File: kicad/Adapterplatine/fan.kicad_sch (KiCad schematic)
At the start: 15 parts, among them J2 Conn_01x05_Pin, J3 Conn_01x04_Pin, J4 Conn_01x03_Pin, X25_1 Conn_01x02_Pin, X36B1 DE9_Socket, X38 Conn_01x02_Pin, X44 Conn_01x05_Pin, X44__g1 Conn_01x02_Pin, X44__r1 Conn_01x04_Pin, X44__y1 Conn_01x02_Pin, X44_b1 Conn_01x04_Pin

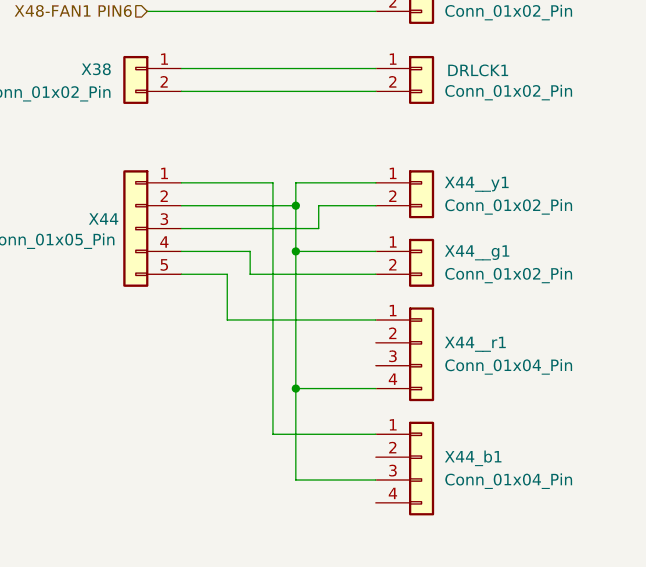
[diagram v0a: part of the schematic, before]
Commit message: Leitungsverlegung Adapterplatine abgeschlossen
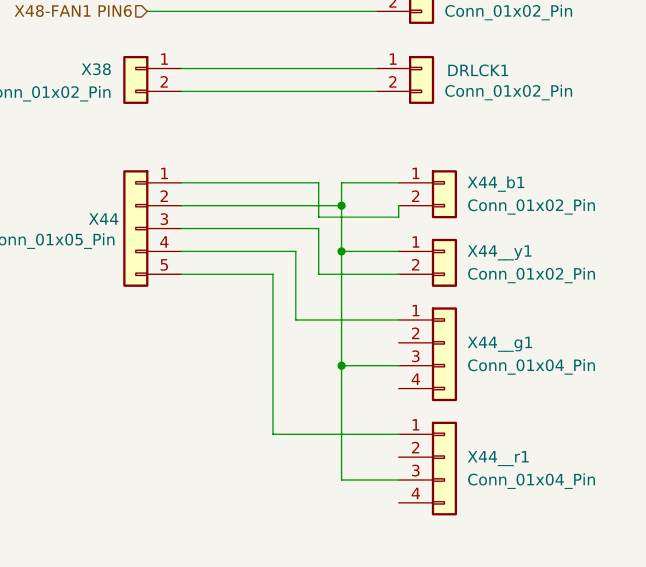
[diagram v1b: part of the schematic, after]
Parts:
- X44__g1: value Conn_01x02_Pin -> Conn_01x04_Pin; footprint Connector_JST:JST_XH_B2B-XH-A_1x02_P2.50mm_Vertical -> Connector_Molex:Molex_KK-254_AE-6410-04A_1x04_P2.54mm_Vertical; symbol Connector_Generic:Conn_01x02 -> Connector_Generic:Conn_01x04
- X44_b1: value Conn_01x04_Pin -> Conn_01x02_Pin; footprint Connector_Molex:Molex_KK-254_AE-6410-04A_1x04_P2.54mm_Vertical -> Connector_JST:JST_XH_B2B-XH-A_1x02_P2.50mm_Vertical; symbol Connector_Generic:Conn_01x04 -> Connector_Generic:Conn_01x02
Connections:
- net at X44.1 (Pin_1): now also X44_b1.2 (Pin_2); no longer X44_b1.1 (Pin_1)
- net at X44.4 (Pin_4): now also X44__g1.1 (Pin_1); no longer X44__g1.2 (Pin_2)
- net at X44__r1.3 (Pin_3): now also X44.2 (Pin_2), X44__g1.3 (Pin_3), X44__y1.1 (Pin_1), X44_b1.1 (Pin_1)
- now unconnected: X44__r1.4 (Pin_4)
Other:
- moved on the sheet: X44__r1, X44__y1

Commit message: Aufnahme des i2C Splitters am Druckkopf/ Kleine Änderungen Platine
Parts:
- renumbered X44_b1 to X44_Buzzer1, X44__y1 to X44__Gelb1, X44__g1 to X44__Grün1, X44__r1 to X44__Rot1
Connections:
- net X48-FAN0 PIN4: now also TOOL-FAN0.2 (Pin_2); no longer TOOL-FAN0.1 (Pin_1)
- net X48-FAN0 PIN9: now also TOOL-FAN0.1 (Pin_1); no longer TOOL-FAN0.2 (Pin_2)
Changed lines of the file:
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@@
+	(wire
+		(pts
+			(xy 204.47 67.31) (xy 229.87 67.31)
+		)
+		(stroke
+			(width 0)
+			(type default)
+		)
+	)
+	(wire
+		(pts
+			(xy 204.47 69.85) (xy 229.87 69.85)
+		)
+		(stroke
+			(width 0)
+			(type default)
+		)
+	)
 	(wire
 		(pts
@@
 	(wire
 		(pts
-			(xy 204.47 69.85) (xy 229.87 69.85)
+			(xy 226.06 100.33) (xy 226.06 102.87)
 		)
 		(stroke
@@
 	(wire
 		(pts
-			(xy 226.06 100.33) (xy 226.06 102.87)
+			(xy 223.52 105.41) (xy 223.52 110.49)
 		)
 		(stroke
@@
 	(wire
 		(pts
-			(xy 223.52 105.41) (xy 223.52 110.49)
+			(xy 226.06 107.95) (xy 226.06 120.65)
 		)
 		(stroke
@@
 	(wire
 		(pts
-			(xy 226.06 107.95) (xy 226.06 120.65)
+			(xy 232.41 104.14) (xy 232.41 102.87)
 		)
 		(stroke
@@
 	(wire
 		(pts
-			(xy 204.47 67.31) (xy 229.87 67.31)
+			(xy 208.28 55.88) (xy 229.87 55.88)
 		)
 		(stroke
@@
 	(wire
 		(pts
-			(xy 232.41 104.14) (xy 232.41 102.87)
+			(xy 204.47 81.28) (xy 229.87 81.28)
 		)
 		(stroke
@@
 	(wire
 		(pts
-			(xy 208.28 55.88) (xy 229.87 55.88)
+			(xy 220.98 115.57) (xy 232.41 115.57)
 		)
 		(stroke
@@
 	(wire
 		(pts
-			(xy 204.47 81.28) (xy 229.87 81.28)
+			(xy 220.98 107.95) (xy 208.28 107.95)
 		)
 		(stroke
@@
 	(wire
 		(pts
-			(xy 220.98 115.57) (xy 232.41 115.57)
+			(xy 220.98 107.95) (xy 220.98 115.57)
 		)
 		(stroke
@@
 		)
 	)
-	(wire
-		(pts
-			(xy 220.98 107.95) (xy 208.28 107.95)
-		)
-		(stroke
-			(width 0)
-			(type default)
-		)
-	)
-	(wire
-		(pts
-			(xy 220.98 107.95) (xy 220.98 115.57)
-		)
-		(stroke
-			(width 0)
-			(type default)
-		)
-	)
 	(hierarchical_label "X48-FAN0 PIN9"
 		(shape input)
-		(at 204.47 69.85 180)
+		(at 204.47 67.31 180)
 		(effects
 			(font
@@
 	(hierarchical_label "X48-FAN0 PIN4"
 		(shape input)
-		(at 204.47 67.31 180)
+		(at 204.47 69.85 180)
 		(effects
 			(font
@@
 		(dnp no)
 		(fields_autoplaced yes)
-		(property "Reference" "X44__y1"
+		(property "Reference" "X44__Gelb1"
 			(at 240.03 107.9499 0)
 			(show_name no)
@@
 			(project "Adapterplatine"
 				(path "/99d5d967-6a35-454f-aac3-01cafa1d30b4/d3c70294-d43c-4ffa-984d-dc715d4de7b5"
-					(reference "X44__y1")
+					(reference "X44__Gelb1")
 					(unit 1)
 				)
@@
 		(dnp no)
 		(fields_autoplaced yes)
-		(property "Reference" "X44_b1"
+		(property "Reference" "X44_Buzzer1"
 			(at 240.03 100.3299 0)
 			(show_name no)
@@
 			(project "Adapterplatine"
 				(path "/99d5d967-6a35-454f-aac3-01cafa1d30b4/d3c70294-d43c-4ffa-984d-dc715d4de7b5"
-					(reference "X44_b1")
+					(reference "X44_Buzzer1")
 					(unit 1)
 				)
@@
 		(dnp no)
 		(fields_autoplaced yes)
-		(property "Reference" "X44__r1"
+		(property "Reference" "X44__Rot1"
 			(at 240.03 130.8099 0)
 			(show_name no)
@@
 			(project "Adapterplatine"
 				(path "/99d5d967-6a35-454f-aac3-01cafa1d30b4/d3c70294-d43c-4ffa-984d-dc715d4de7b5"
-					(reference "X44__r1")
+					(reference "X44__Rot1")
 					(unit 1)
 				)
@@
 		(dnp no)
 		(fields_autoplaced yes)
-		(property "Reference" "X44__g1"
+		(property "Reference" "X44__Grün1"
 			(at 240.03 118.1099 0)
 			(show_name no)
@@
 			(project "Adapterplatine"
 				(path "/99d5d967-6a35-454f-aac3-01cafa1d30b4/d3c70294-d43c-4ffa-984d-dc715d4de7b5"
-					(reference "X44__g1")
+					(reference "X44__Grün1")
 					(unit 1)
 				)

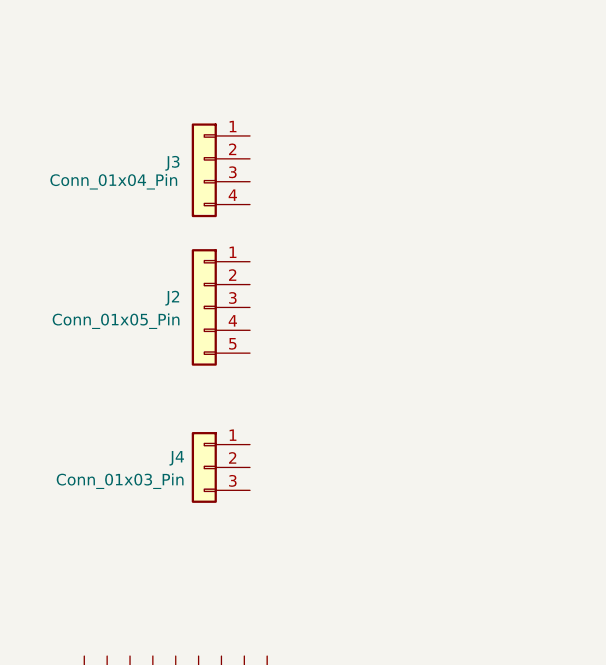
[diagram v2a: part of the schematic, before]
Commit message: Einbau Vakuum Pumpe/ Einzeichnung Kraken benutze Pins
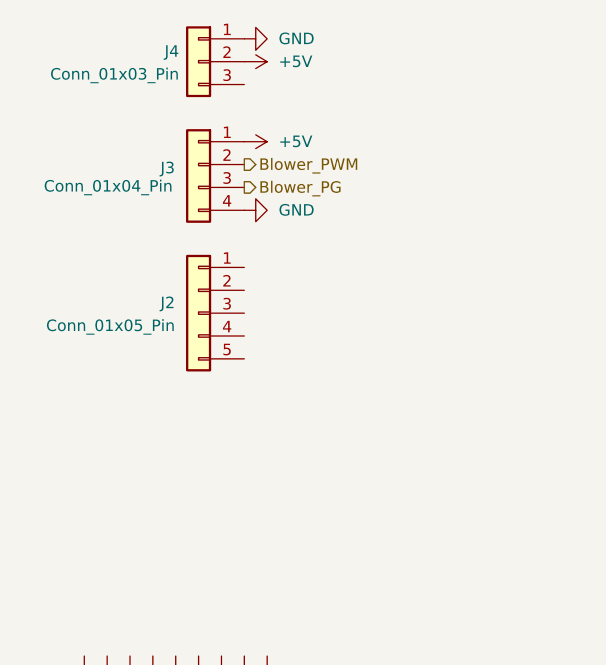
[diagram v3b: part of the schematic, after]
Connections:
- net GND: now reaches J4.1 (Pin_1)
- net GND: now also J3.4 (Pin_4)
- net +5V: now reaches J4.2 (Pin_2)
- net +5V: now also J3.1 (Pin_1)
- net Blower_PWM: now reaches J3.2 (Pin_2)
- net Blower_PG: now reaches J3.3 (Pin_3)
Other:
- moved on the sheet: J2, J3, J4

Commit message: Abschlussbericht angefangen/ Adapterplatine ECR DCR
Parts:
- added ChamberFAN1: Conn_01x02_Pin, Connector_JST:JST_XH_B2B-XH-A_1x02_P2.50mm_Vertical, symbol Connector_Generic:Conn_01x02
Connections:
- net GND: now also J4.3 (Pin_3), X36B1.SH (PAD), ChamberFAN1.2 (Pin_2); no longer J4.1 (Pin_1)
- net X48-FAN0 PIN9: no longer names the net of TOOL-FAN0.1 (Pin_1)
- net X48-FAN1 PIN9: no longer names the net of TOOL-FAN1.1 (Pin_1)
- new net: ChamberFAN1.1 (Pin_1), J4.1 (Pin_1)
- new net: X44.2 (Pin_2), X44_Buzzer1.1 (Pin_1)
- now unconnected: X44__Gelb1.1 (Pin_1), X44__Grün1.3 (Pin_3), X44__Rot1.3 (Pin_3)
- no-connect marks 0 -> 23
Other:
- moved on the sheet: J4

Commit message: Adapterplatine Version 1.0 final
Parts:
- renumbered X44_Buzzer1 to X44_B1, X44__Grün1 to X44_G1, X44__Rot1 to X44_R1, X44__Gelb1 to X44_Y1
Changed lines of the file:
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@@
 		(dnp no)
 		(fields_autoplaced yes)
-		(property "Reference" "X44__Gelb1"
+		(property "Reference" "X44_Y1"
 			(at 240.03 107.9499 0)
 			(show_name no)
@@
 			(project "Adapterplatine"
 				(path "/99d5d967-6a35-454f-aac3-01cafa1d30b4/d3c70294-d43c-4ffa-984d-dc715d4de7b5"
-					(reference "X44__Gelb1")
+					(reference "X44_Y1")
 					(unit 1)
 				)
@@
 		(dnp no)
 		(fields_autoplaced yes)
-		(property "Reference" "X44_Buzzer1"
+		(property "Reference" "X44_B1"
 			(at 240.03 100.3299 0)
 			(show_name no)
@@
 			(project "Adapterplatine"
 				(path "/99d5d967-6a35-454f-aac3-01cafa1d30b4/d3c70294-d43c-4ffa-984d-dc715d4de7b5"
-					(reference "X44_Buzzer1")
+					(reference "X44_B1")
 					(unit 1)
 				)
@@
 		(dnp no)
 		(fields_autoplaced yes)
-		(property "Reference" "X44__Rot1"
+		(property "Reference" "X44_R1"
 			(at 240.03 130.8099 0)
 			(show_name no)
@@
 			(project "Adapterplatine"
 				(path "/99d5d967-6a35-454f-aac3-01cafa1d30b4/d3c70294-d43c-4ffa-984d-dc715d4de7b5"
-					(reference "X44__Rot1")
+					(reference "X44_R1")
 					(unit 1)
 				)
@@
 		(dnp no)
 		(fields_autoplaced yes)
-		(property "Reference" "X44__Grün1"
+		(property "Reference" "X44_G1"
 			(at 240.03 118.1099 0)
 			(show_name no)
@@
 			(project "Adapterplatine"
 				(path "/99d5d967-6a35-454f-aac3-01cafa1d30b4/d3c70294-d43c-4ffa-984d-dc715d4de7b5"
-					(reference "X44__Grün1")
+					(reference "X44_G1")
 					(unit 1)
 				)
